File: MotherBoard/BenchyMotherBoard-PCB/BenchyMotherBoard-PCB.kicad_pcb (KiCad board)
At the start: 8 copper layers, 160 x 100 mm, 358 parts, among them J1 PWR-CONN, J10 USB3_B, J11 USB3-PORT2, J12 USB3-PORT3, J13 USB3-PORT4, J14 USB3-PORT5, J15 USB-INTERNAL-PORT1, J16 TFT-DISPLAY, J17 USB-INTERNAL-PORT2, J18 COMMS-PWR, J19 COMMS-ELOAD, J2 SWD-TAG, J20 COMMS-SWITCHER, J21 RELAYS-CONN, J22 COMMS-LOGIC, J3 FILES-SD-CARD, J4 BOOT0-CONN, J5 BOOT1-CONN, J6 BOOT2-CONN, J7 BOOT-SD-CARD, J8 FAN-CONN, J9 USB3-PORT1, Q1 SQ2310ES_SOT23, Q2 MMBT2222A, Q3 RQ5A030AP, U1 STM32MP157FAB1, U10 USB7206C, U11 IS43TR16256B-125KBLI, U12 UCS2114, U13 UCS2114, U14 UCS2114, U15 LM317L, U16 AS321, U17 24LC08, U18 USB2412, U2 TPS65400RGZT, U3 NCP51200, U4 ATTINY416-MNR, U5 MAX15027, U6 MAX15027, U7 SN74LVC1G32, U8 74HCT2G08, U9 AP2127K-3.3, Y1 24MHz, Y2 32.7KHz, Y3 25MHz, Y4 25MHz

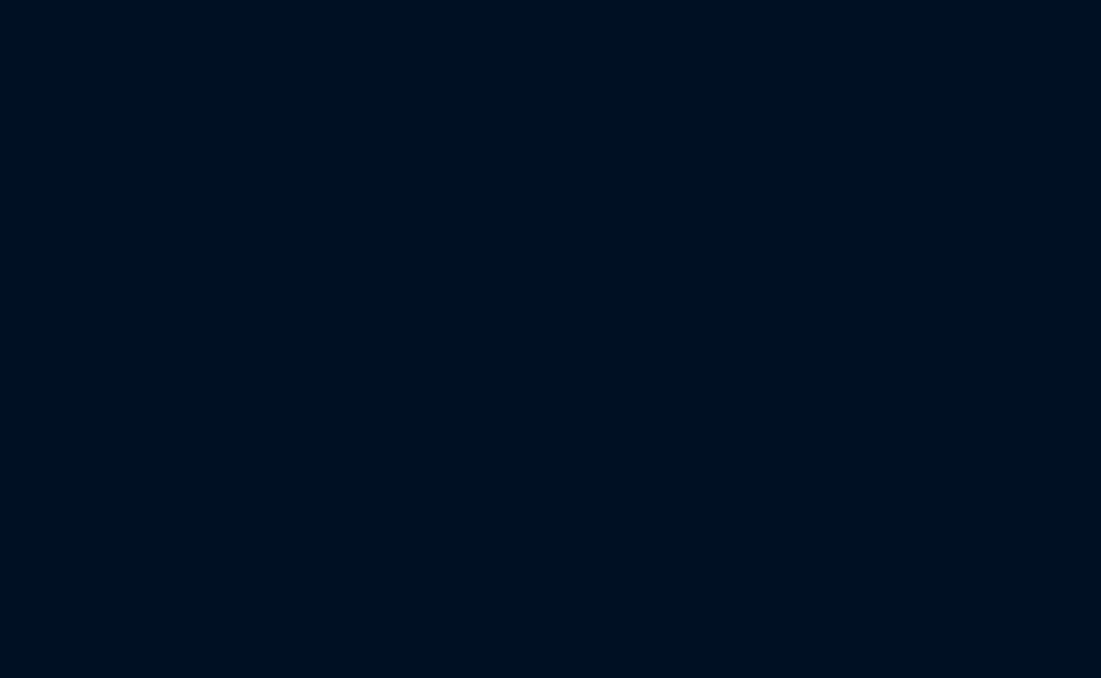
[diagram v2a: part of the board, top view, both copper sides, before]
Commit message: Add PGOOD led and replace PWR switch
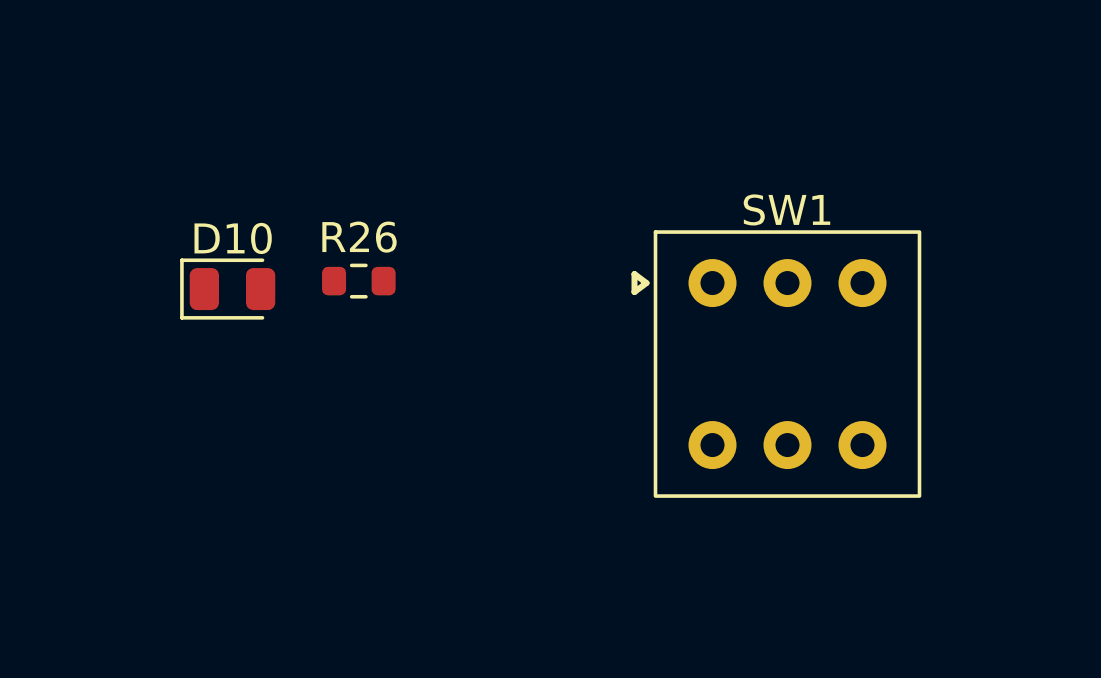
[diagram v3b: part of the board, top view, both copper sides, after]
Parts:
- added D10: GREEN, LED_SMD:LED_0805_2012Metric, F.Cu at (140.5, 157.2)
- added R26: 500, Resistor_SMD:R_0603_1608Metric, F.Cu at (144.7, 157.0)
- added SW1: SW_DPDT_x2, Daxxn_Switches:PHAP4383V, F.Cu at (159.0, 159.8)
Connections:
- R25 pad 2: /POWER/VDD-DDR-PG -> /POWER/VTT-DDR-PG
- U3 pad 9: /POWER/VDD-DDR-PG -> /POWER/VTT-DDR-PG
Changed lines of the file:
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@@
   (net 402 "Net-(C39-Pad2)")
   (net 403 "Net-(C174-Pad1)")
+  (net 404 "/POWER/VTT-DDR-PG")
+  (net 405 "unconnected-(SW1-Pad1)")
+  (net 406 "unconnected-(SW1-Pad2)")
+  (net 407 "unconnected-(SW1-Pad3)")
+  (net 408 "unconnected-(SW1-Pad4)")
+  (net 409 "unconnected-(SW1-Pad5)")
+  (net 410 "unconnected-(SW1-Pad6)")
+  (net 411 "Net-(D10-Pad1)")
   (footprint "Capacitor_SMD:C_1210_3225Metric" (layer "F.Cu")
     (at 118 318)
@@
       (net 192 "VDD") (pintype "passive"))
     (pad "2" smd roundrect (at 0.51 0 270) (size 0.54 0.64) (layers "F.Cu" "F.Paste" "F.Mask") (roundrect_rratio 0.25)
-      (net 168 "/POWER/VDD-DDR-PG") (pintype "passive"))
+      (net 404 "/POWER/VTT-DDR-PG") (pintype "passive"))
     (model "${KICAD6_3DMODEL_DIR}/Resistor_SMD.3dshapes/R_0402_1005Metric.wrl"
       (offset (xyz 0 0 0))
@@
     (fp_line (start -1.5 -0.5) (end -0.5 -1.5) (layer "F.Fab") (width 0.15))
     (pad "1" smd rect (at -2.15 -0.975) (size 1.1 0.4) (layers "F.Cu" "F.Paste" "F.Mask")
-      (net 183 "unconnected-(U8-Pad1)") (pinfunction "A") (pintype "input+no_connect"))
+      (net 183 "unconnected-(U8-Pad1)") (pinfunction "A") (pintype "input"))
     (pad "2" smd rect (at -2.15 -0.325) (size 1.1 0.4) (layers "F.Cu" "F.Paste" "F.Mask")
-      (net 184 "unconnected-(U8-Pad2)") (pinfunction "B") (pintype "input+no_connect"))
+      (net 184 "unconnected-(U8-Pad2)") (pinfunction "B") (pintype "input"))
     (pad "3" smd rect (at -2.15 0.325) (size 1.1 0.4) (layers "F.Cu" "F.Paste" "F.Mask")
       (net 25 "/POWER/ALL-PGOOD") (pinfunction "Y") (pintype "output"))
@@
       (net 53 "/POWER/SMPS-PGOOD") (pinfunction "B") (pintype "input"))
     (pad "7" smd rect (at 2.15 -0.325) (size 1.1 0.4) (layers "F.Cu" "F.Paste" "F.Mask")
-      (net 185 "unconnected-(U8-Pad7)") (pinfunction "Y") (pintype "output+no_connect"))
+      (net 185 "unconnected-(U8-Pad7)") (pinfunction "Y") (pintype "output"))
     (pad "8" smd rect (at 2.15 -0.975) (size 1.1 0.4) (layers "F.Cu" "F.Paste" "F.Mask")
       (net 3 "VDD-PWR") (pintype "power_in"))
@@
     )
   )
+  (footprint "Resistor_SMD:R_0603_1608Metric" (layer "F.Cu")
+    (at 144.71 156.985)
+    (descr "Resistor SMD 0603 (1608 Metric), square (rectangular) end terminal, IPC_7351 nominal, (Body size source: IPC-SM-782 page 72, https://www.pcb-3d.com/wordpress/wp-content/uploads/ipc-sm-782a_amendment_1_and_2.pdf), generated with kicad-footprint-generator")
+    (tags "resistor")
+    (property "Sheetfile" "power.kicad_sch")
+    (property "Sheetname" "POWER")
+    (attr smd)
+    (fp_text reference "R26" (at 0 -1.43) (layer "F.SilkS")
+      (effects (font (size 1 1) (thickness 0.15)))
+    )
+    (fp_text value "500" (at 0 1.43) (layer "F.Fab")
+      (effects (font (size 1 1) (thickness 0.15)))
+    )
+    (fp_text user "${REFERENCE}" (at 0 0) (layer "F.Fab")
+      (effects (font (size 0.4 0.4) (thickness 0.06)))
+    )
+    (fp_line (start -0.237258 -0.5225) (end 0.237258 -0.5225) (layer "F.SilkS") (width 0.12))
+    (fp_line (start -0.237258 0.5225) (end 0.237258 0.5225) (layer "F.SilkS") (width 0.12))
+    (fp_line (start -1.48 0.73) (end -1.48 -0.73) (layer "F.CrtYd") (width 0.05))
+    (fp_line (start 1.48 0.73) (end -1.48 0.73) (layer "F.CrtYd") (width 0.05))
+    (fp_line (start 1.48 -0.73) (end 1.48 0.73) (layer "F.CrtYd") (width 0.05))
+    (fp_line (start -1.48 -0.73) (end 1.48 -0.73) (layer "F.CrtYd") (width 0.05))
+    (fp_line (start -0.8 -0.4125) (end 0.8 -0.4125) (layer "F.Fab") (width 0.1))
+    (fp_line (start 0.8 -0.4125) (end 0.8 0.4125) (layer "F.Fab") (width 0.1))
+    (fp_line (start 0.8 0.4125) (end -0.8 0.4125) (layer "F.Fab") (width 0.1))
+    (fp_line (start -0.8 0.4125) (end -0.8 -0.4125) (layer "F.Fab") (width 0.1))
+    (pad "1" smd roundrect (at -0.825 0) (size 0.8 0.95) (layers "F.Cu" "F.Paste" "F.Mask") (roundrect_rratio 0.25)
+      (net 411 "Net-(D10-Pad1)") (pintype "passive"))
+    (pad "2" smd roundrect (at 0.825 0) (size 0.8 0.95) (layers "F.Cu" "F.Paste" "F.Mask") (roundrect_rratio 0.25)
+      (net 2 "GND") (pintype "passive"))
+    (model "${KICAD6_3DMODEL_DIR}/Resistor_SMD.3dshapes/R_0603_1608Metric.wrl"
+      (offset (xyz 0 0 0))
+      (scale (xyz 1 1 1))
+      (rotate (xyz 0 0 0))
+    )
+  )
   (footprint "Daxxn_Connectors:GSB4116341HR" (layer "F.Cu")
     (at 74.407378 267.131901)
@@
       (net 2 "GND") (pinfunction "GND") (pintype "power_in"))
     (pad "9" smd roundrect (at 1.4625 -0.5) (size 0.825 0.25) (layers "F.Cu" "F.Paste" "F.Mask") (roundrect_rratio 0.25)
-      (net 168 "/POWER/VDD-DDR-PG") (pinfunction "PGOOD") (pintype "output"))
+      (net 404 "/POWER/VTT-DDR-PG") (pinfunction "PGOOD") (pintype "output"))
     (pad "10" smd roundrect (at 1.4625 -1) (size 0.825 0.25) (layers "F.Cu" "F.Paste" "F.Mask") (roundrect_rratio 0.25)
       (net 192 "VDD") (pinfunction "AIN") (pintype "input"))
@@
     )
   )
+  (footprint "LED_SMD:LED_0805_2012Metric" (layer "F.Cu")
+    (at 140.5 157.25)
+    (descr "LED SMD 0805 (2012 Metric), square (rectangular) end terminal, IPC_7351 nominal, (Body size source: https://docs.google.com/spreadsheets/d/1BsfQQcO9C6DZCsRaXUlFlo91Tg2WpOkGARC1WS5S8t0/edit?usp=sharing), generated with kicad-footprint-generator")
+    (tags "LED")
+    (property "Sheetfile" "power.kicad_sch")
+    (property "Sheetname" "POWER")
+    (attr smd)
+    (fp_text reference "D10" (at 0 -1.65) (layer "F.SilkS")
+      (effects (font (size 1 1) (thickness 0.15)))
+    )
+    (fp_text value "GREEN" (at 0 1.65) (layer "F.Fab")
+      (effects (font (size 1 1) (thickness 0.15)))
+    )
+    (fp_text user "${REFERENCE}" (at 0 0) (layer "F.Fab")
+      (effects (font (size 0.5 0.5) (thickness 0.08)))
+    )
+    (fp_line (start -1.685 0.96) (end 1 0.96) (layer "F.SilkS") (width 0.12))
+    (fp_line (start -1.685 -0.96) (end -1.685 0.96) (layer "F.SilkS") (width 0.12))
+    (fp_line (start 1 -0.96) (end -1.685 -0.96) (layer "F.SilkS") (width 0.12))
+    (fp_line (start 1.68 -0.95) (end 1.68 0.95) (layer "F.CrtYd") (width 0.05))
+    (fp_line (start -1.68 0.95) (end -1.68 -0.95) (layer "F.CrtYd") (width 0.05))
+    (fp_line (start -1.68 -0.95) (end 1.68 -0.95) (layer "F.CrtYd") (width 0.05))
+    (fp_line (start 1.68 0.95) (end -1.68 0.95) (layer "F.CrtYd") (width 0.05))
+    (fp_line (start 1 -0.6) (end -0.7 -0.6) (layer "F.Fab") (width 0.1))
+    (fp_line (start 1 0.6) (end 1 -0.6) (layer "F.Fab") (width 0.1))
+    (fp_line (start -1 -0.3) (end -1 0.6) (layer "F.Fab") (width 0.1))
+    (fp_line (start -1 0.6) (end 1 0.6) (layer "F.Fab") (width 0.1))
+    (fp_line (start -0.7 -0.6) (end -1 -0.3) (layer "F.Fab") (width 0.1))
+    (pad "1" smd roundrect (at -0.9375 0) (size 0.975 1.4) (layers "F.Cu" "F.Paste" "F.Mask") (roundrect_rratio 0.25)
+      (net 411 "Net-(D10-Pad1)") (pinfunction "K") (pintype "passive"))
+    (pad "2" smd roundrect (at 0.9375 0) (size 0.975 1.4) (layers "F.Cu" "F.Paste" "F.Mask") (roundrect_rratio 0.25)
+      (net 25 "/POWER/ALL-PGOOD") (pinfunction "A") (pintype "passive"))
+    (model "${KICAD6_3DMODEL_DIR}/LED_SMD.3dshapes/LED_0805_2012Metric.wrl"
+      (offset (xyz 0 0 0))
+      (scale (xyz 1 1 1))
+      (rotate (xyz 0 0 0))
+    )
+  )
   (footprint "Resistor_SMD:R_0402_1005Metric" (layer "F.Cu")
     (at 90.25 217)
@@
       (offset (xyz 0 0 0))
       (scale (xyz 1 1 1))
+      (rotate (xyz 0 0 0))
+    )
+  )
+  (footprint "Daxxn_Switches:PHAP4383V" (layer "F.Cu")
+    (at 159 159.75)
+    (property "Sheetfile" "power.kicad_sch")
+    (property "Sheetname" "POWER")
+    (attr through_hole)
+    (fp_text reference "SW1" (at 0 -5.1 unlocked) (layer "F.SilkS")
+      (effects (font (size 1 1) (thickness 0.15)))
+    )
+    (fp_text value "SW_DPDT_x2" (at 0 0.7 unlocked) (layer "F.Fab")
+      (effects (font (size 0.75 0.75) (thickness 0.1875)))
+    )
+    (fp_text user "${REFERENCE}" (at 0 -0.6 unlocked) (layer "F.Fab")
+      (effects (font (size 0.75 0.75) (thickness 0.15)))
+    )
+    (fp_line (start -5.1 -2.4) (end -4.7 -2.7) (layer "F.SilkS") (width 0.2))
+    (fp_line (start -5.1 -3) (end -5.1 -2.4) (layer "F.SilkS") (width 0.2))
+    (fp_line (start -4.7 -2.7) (end -5.1 -3) (layer "F.SilkS") (width 0.2))
+    (fp_rect (start -4.4 -4.4) (end 4.4 4.4) (layer "F.SilkS") (width 0.12) (fill none))
+    (fp_rect (start -4.25 -4.25) (end 4.25 4.25) (layer "F.Fab") (width 0.1) (fill none))
+    (pad "1" thru_hole circle (at -2.5 -2.7) (size 1.6 1.6) (drill 0.8) (layers *.Cu *.Mask)
+      (net 405 "unconnected-(SW1-Pad1)") (pinfunction "A") (pintype "passive"))
+    (pad "2" thru_hole circle (at 0 -2.7) (size 1.6 1.6) (drill 0.8) (layers *.Cu *.Mask)
+      (net 406 "unconnected-(SW1-Pad2)") (pinfunction "B") (pintype "passive"))
+    (pad "3" thru_hole circle (at 2.5 -2.7) (size 1.6 1.6) (drill 0.8) (layers *.Cu *.Mask)
+      (net 407 "unconnected-(SW1-Pad3)") (pinfunction "C") (pintype "passive"))
+    (pad "4" thru_hole circle (at -2.5 2.7) (size 1.6 1.6) (drill 0.8) (layers *.Cu *.Mask)
+      (net 408 "unconnected-(SW1-Pad4)") (pinfunction "A") (pintype "passive"))
+    (pad "5" thru_hole circle (at 0 2.7) (size 1.6 1.6) (drill 0.8) (layers *.Cu *.Mask)
+      (net 409 "unconnected-(SW1-Pad5)") (pinfunction "B") (pintype "passive"))
+    (pad "6" thru_hole circle (at 2.5 2.7) (size 1.6 1.6) (drill 0.8) (layers *.Cu *.Mask)
+      (net 410 "unconnected-(SW1-Pad6)") (pinfunction "C") (pintype "passive"))
+    (model "${ENGINEERING}/KiCad/Libraries/Models/Controls/PHAP4383V.stp"
+      (offset (xyz 0 0 0))
+      (scale (xyz 1 1 1))
